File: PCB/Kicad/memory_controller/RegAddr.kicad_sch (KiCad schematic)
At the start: 4 parts, among them U11 74LS377, U12 74LS377

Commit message: fix
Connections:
- net nCLKen renamed ~{CLK_en}
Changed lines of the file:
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@@
 		)
 	)
-	(hierarchical_label "nCLKen"
+	(hierarchical_label "~{CLK_en}"
 		(shape input)
 		(at 129.54 78.74 180)
-		(effects
-			(font
-				(size 1.27 1.27)
-			)
-			(justify right)
-		)
-	)
-	(hierarchical_label "nCLKen"
-		(shape input)
-		(at 128.27 130.81 180)
 		(effects
 			(font
@@
 		(effects
 			(font
+				(size 1.27 1.27)
+			)
+			(justify right)
+		)
+	)
+	(hierarchical_label "~{CLK_en}"
+		(shape input)
+		(at 128.27 130.81 180)
+		(effects
+			(font

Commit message: pcb init
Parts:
- C11, C12: footprint (none) -> Capacitor_SMD:C_0402_1005Metric
- U11, U12: footprint (none) -> Package_SO:SSOP-20_5.3x7.2mm_P0.65mm
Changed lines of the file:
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@@
 			)
 		)
-		(property "Footprint" ""
+		(property "Footprint" "Package_SO:SSOP-20_5.3x7.2mm_P0.65mm"
 			(at 146.05 118.11 0)
 			(effects
@@
 			)
 		)
-		(property "Footprint" ""
+		(property "Footprint" "Package_SO:SSOP-20_5.3x7.2mm_P0.65mm"
 			(at 146.05 66.04 0)
 			(effects
@@
 			)
 		)
-		(property "Footprint" ""
+		(property "Footprint" "Capacitor_SMD:C_0402_1005Metric"
 			(at 161.5948 78.74 0)
 			(effects
@@
 			)
 		)
-		(property "Footprint" ""
+		(property "Footprint" "Capacitor_SMD:C_0402_1005Metric"
 			(at 134.9248 140.97 0)
 			(effects

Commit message: LEDs + minor fixes
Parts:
- added Dr0, Dr1, Dr10, Dr11, Dr12, Dr13, Dr14, Dr15, Dr2, Dr3, Dr4, Dr5, Dr6, Dr7, Dr8, Dr9: red, LED_SMD:LED_0603_1608Metric, symbol Device:LED
- added Rr0, Rr1, Rr10, Rr11, Rr12, Rr13, Rr14, Rr15, Rr2, Rr3, Rr4, Rr5, Rr6, Rr7, Rr8, Rr9: 680, Resistor_SMD:R_0402_1005Metric, symbol Device:R
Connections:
- net DATA_OUT0: now also Dr0.2 (A)
- net DATA_OUT1: now also Dr1.2 (A)
- net DATA_OUT10: now also Dr10.2 (A)
- net DATA_OUT11: now also Dr11.2 (A)
- net DATA_OUT12: now also Dr12.2 (A)
- net DATA_OUT13: now also Dr13.2 (A)
- net DATA_OUT14: now also Dr14.2 (A)
- net DATA_OUT15: now also Dr15.2 (A)
- net DATA_OUT2: now also Dr2.2 (A)
- net DATA_OUT3: now also Dr3.2 (A)
- net DATA_OUT4: now also Dr4.2 (A)
- net DATA_OUT5: now also Dr5.2 (A)
- net DATA_OUT6: now also Dr6.2 (A)
- net DATA_OUT7: now also Dr7.2 (A)
- net DATA_OUT8: now also Dr8.2 (A)
- net DATA_OUT9: now also Dr9.2 (A)
- net GND: now also Rr0.2, Rr1.2, Rr10.2, Rr11.2, Rr12.2, Rr13.2, Rr14.2, Rr15.2, Rr2.2, Rr3.2, Rr4.2, Rr5.2, Rr6.2, Rr7.2, Rr8.2, Rr9.2
- new net: Dr10.1 (K), Rr10.1
- new net: Dr2.1 (K), Rr2.1
- new net: Dr12.1 (K), Rr12.1
- new net: Dr6.1 (K), Rr6.1
- new net: Dr15.1 (K), Rr15.1
- new net: Dr13.1 (K), Rr13.1
- new net: Dr11.1 (K), Rr11.1
- new net: Dr5.1 (K), Rr5.1
- new net: Dr3.1 (K), Rr3.1
- new net: Dr0.1 (K), Rr0.1
- new net: Dr7.1 (K), Rr7.1
- new net: Dr4.1 (K), Rr4.1
- new net: Dr8.1 (K), Rr8.1
- new net: Dr14.1 (K), Rr14.1
- new net: Dr1.1 (K), Rr1.1
- new net: Dr9.1 (K), Rr9.1
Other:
- moved on the sheet: C11, C12, U11, U12

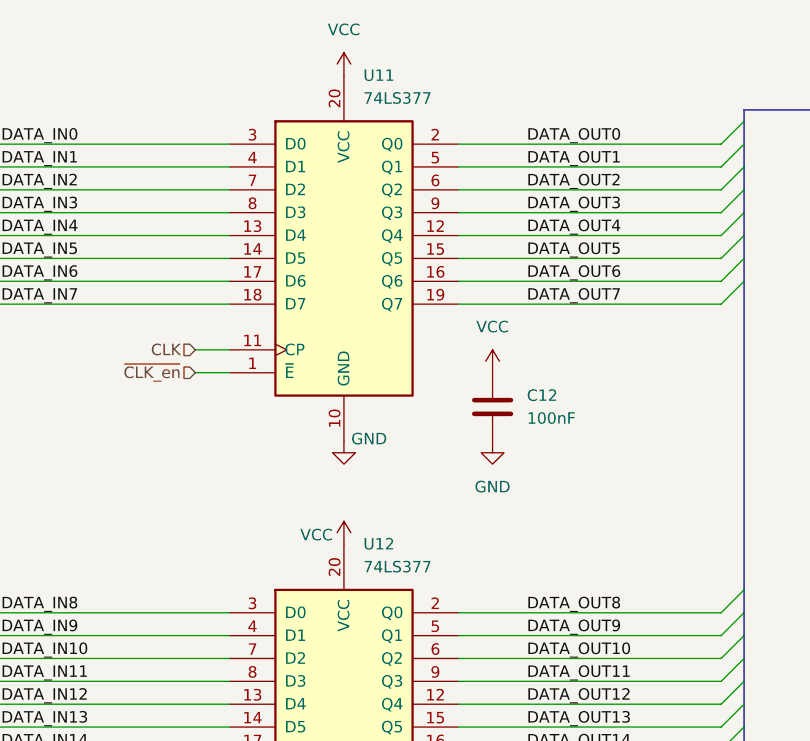
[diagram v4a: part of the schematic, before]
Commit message: memory controller schematic update
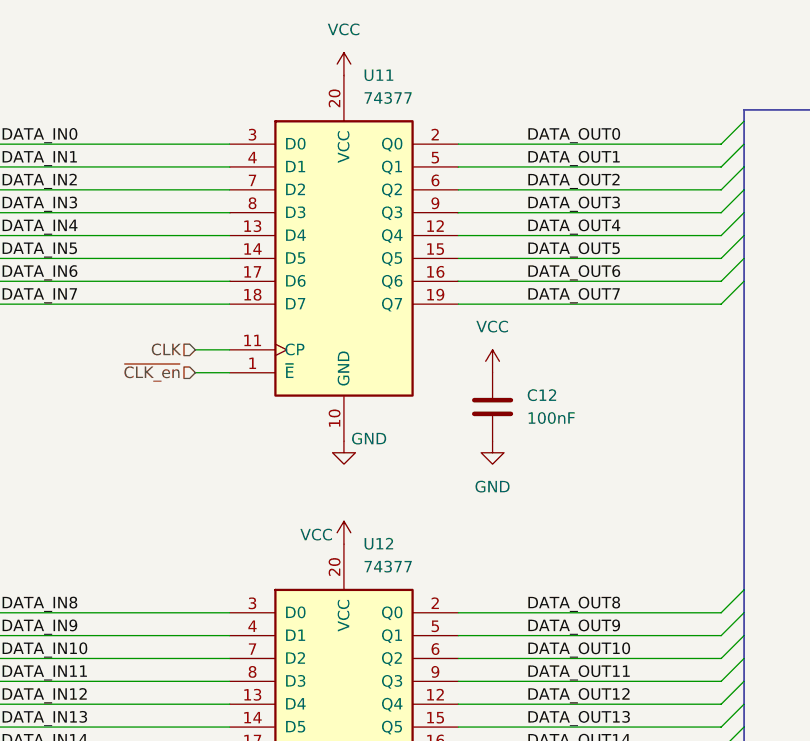
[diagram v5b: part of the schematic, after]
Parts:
- U11, U12: value 74LS377 -> 74377
